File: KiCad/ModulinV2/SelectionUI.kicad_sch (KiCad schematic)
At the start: 43 parts, among them IC33 CD4028BM96, Q10 BC847B,215, Q11 BC847B,215, Q12 BC847B,215, Q13 BC847B,215, Q14 BC847B,215, Q15 BC847B,215, Q16 BC847B,215, Q17 BC847B,215, Q8 BC847B,215, Q9 BC847B,215

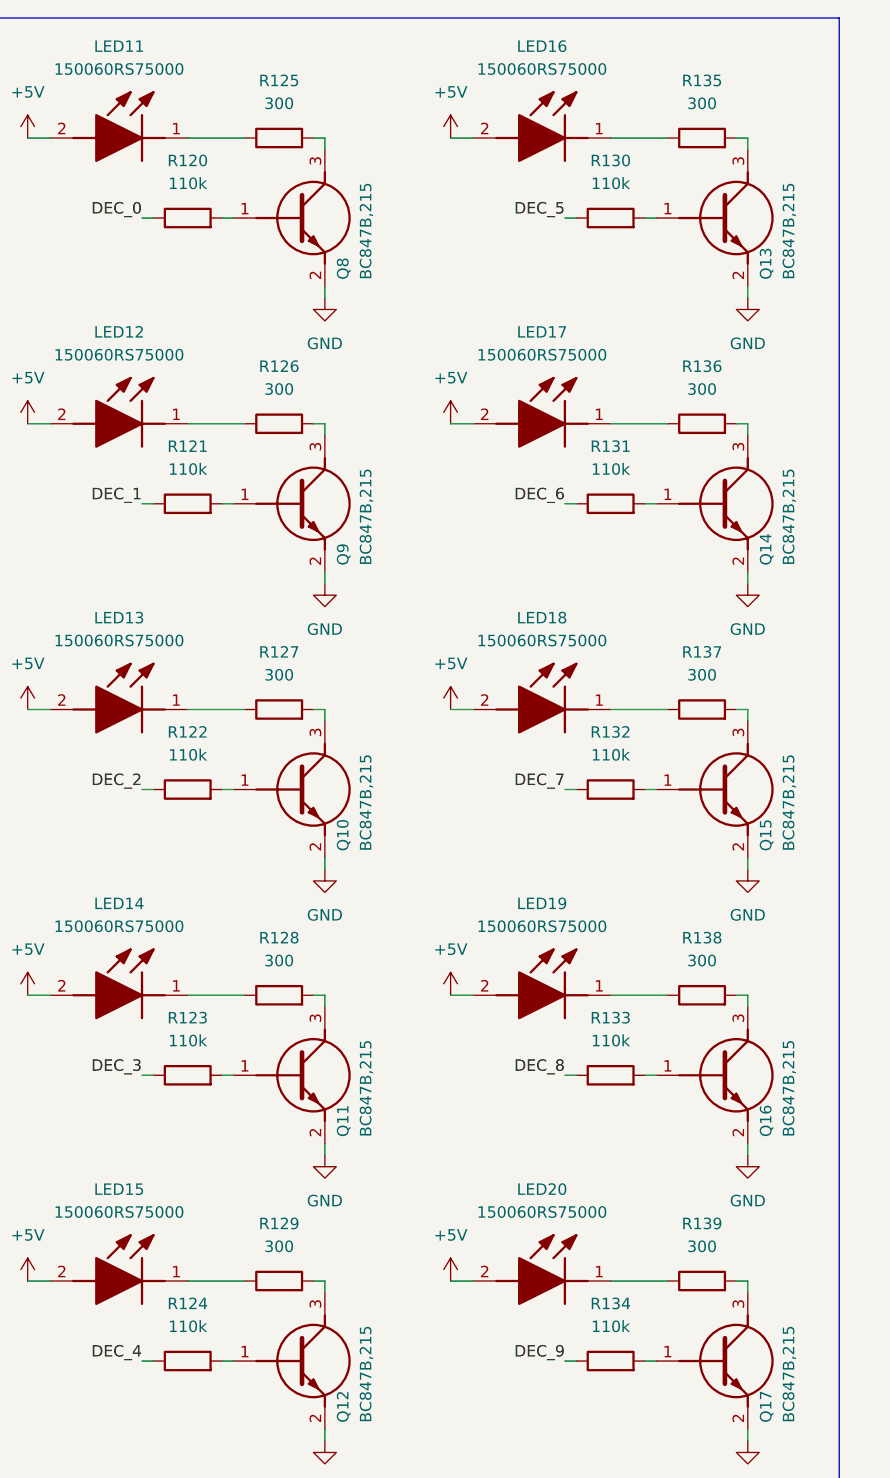
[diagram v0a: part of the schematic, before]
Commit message: Added 4k7 pullups to I2C lines
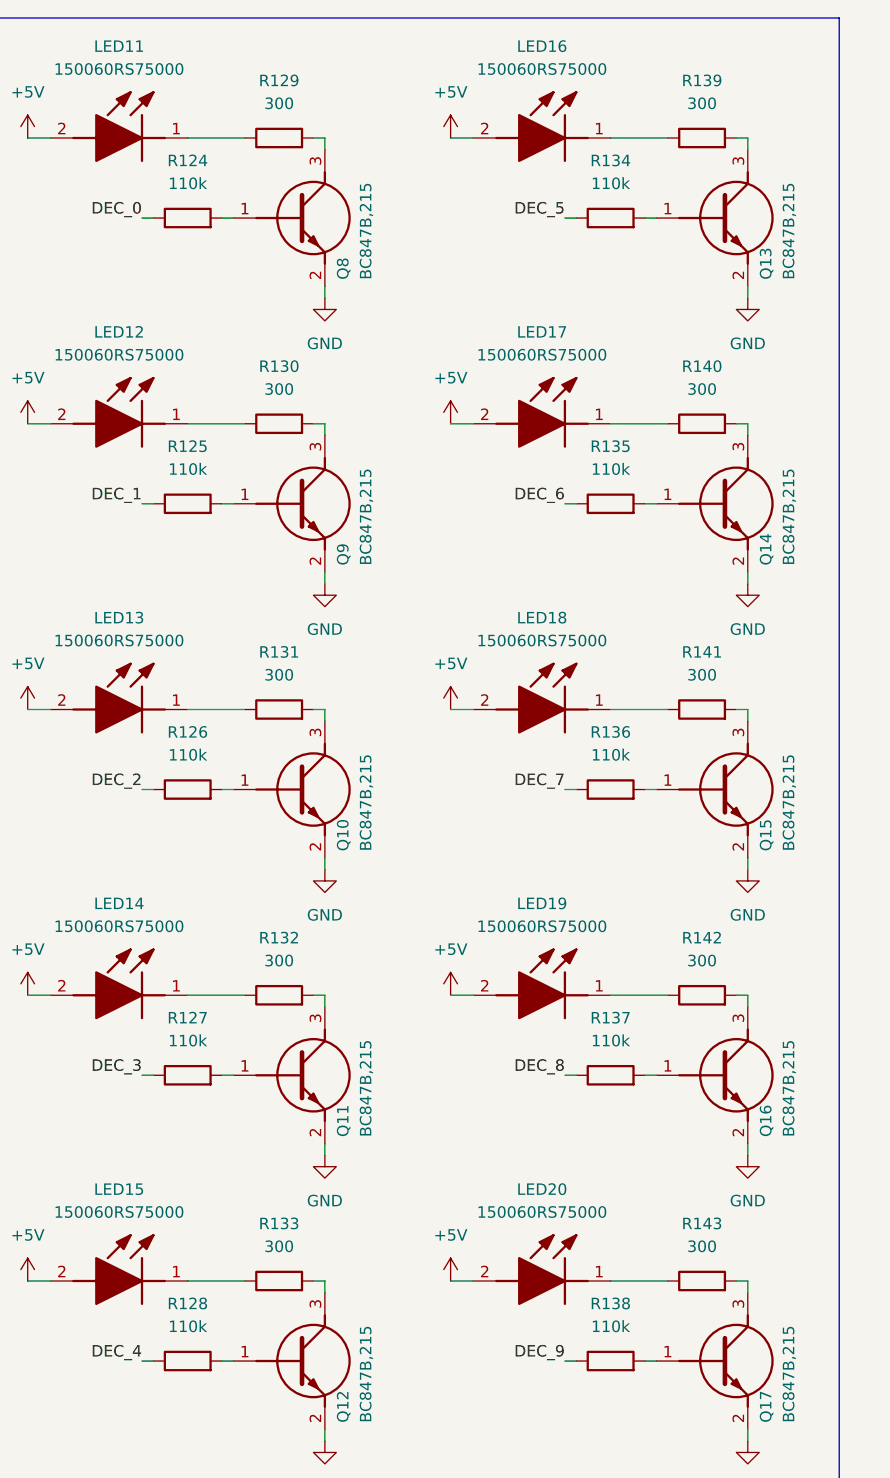
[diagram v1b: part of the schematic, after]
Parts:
- renumbered R120 to R124, R121 to R125, R122 to R126, R123 to R127, R124 to R128, R125 to R129, R126 to R130, R127 to R131, R128 to R132, R129 to R133, R130 to R134, R131 to R135, R132 to R136, R133 to R137, R134 to R138, R135 to R139, R136 to R140, R137 to R141, R138 to R142, R139 to R143

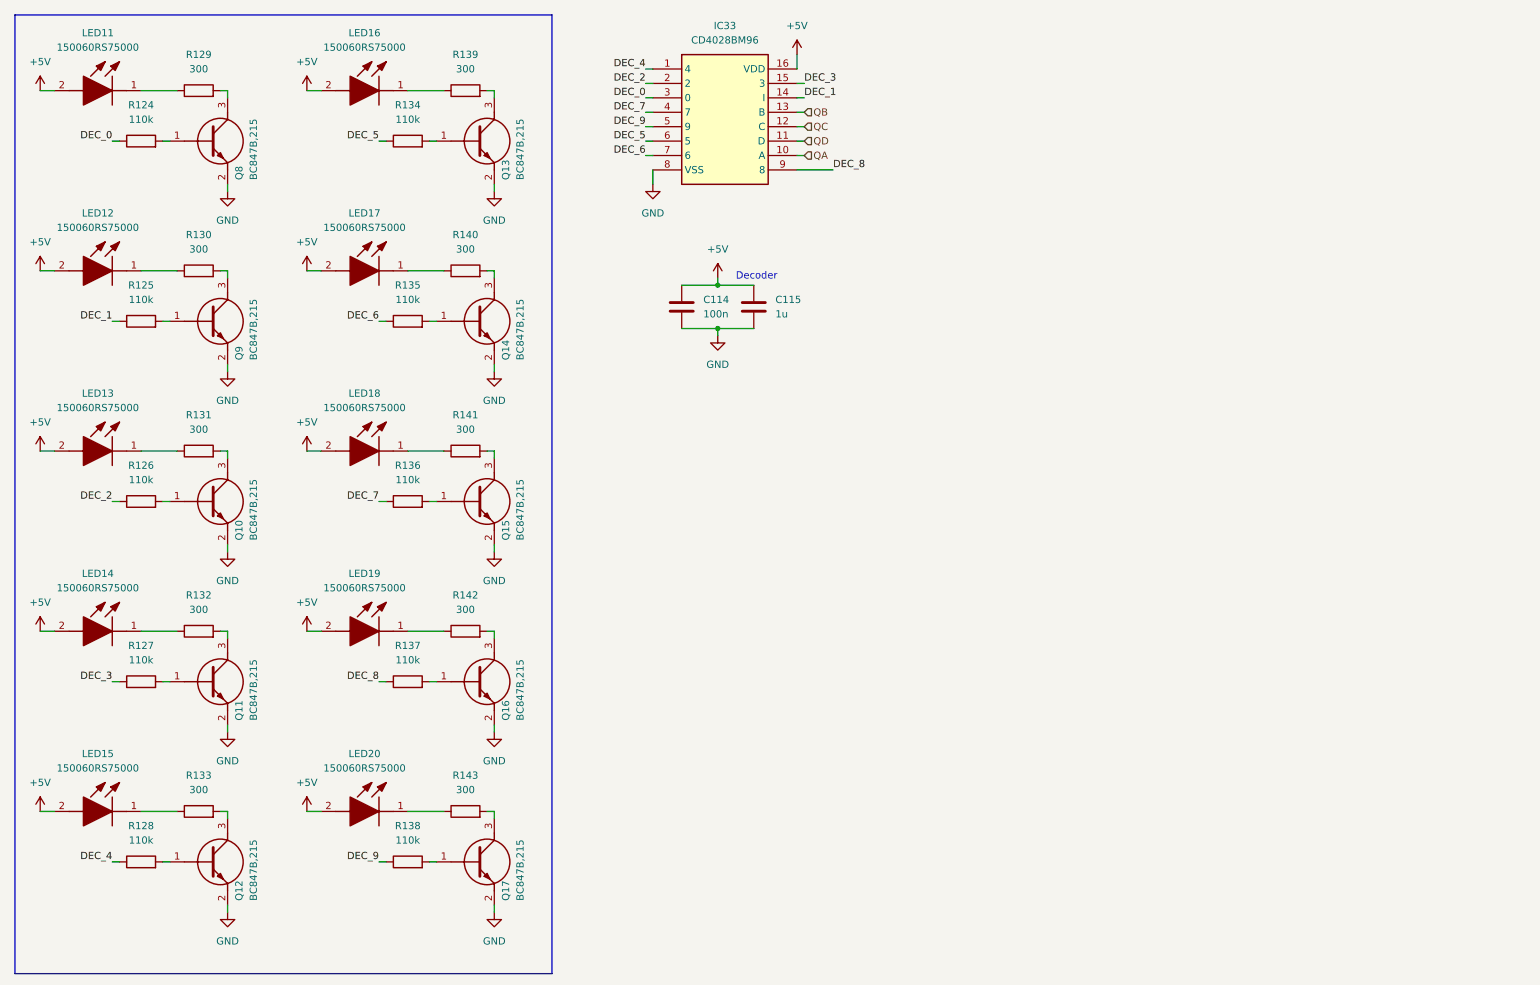
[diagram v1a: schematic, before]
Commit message: Added wave selection jumpers for testing
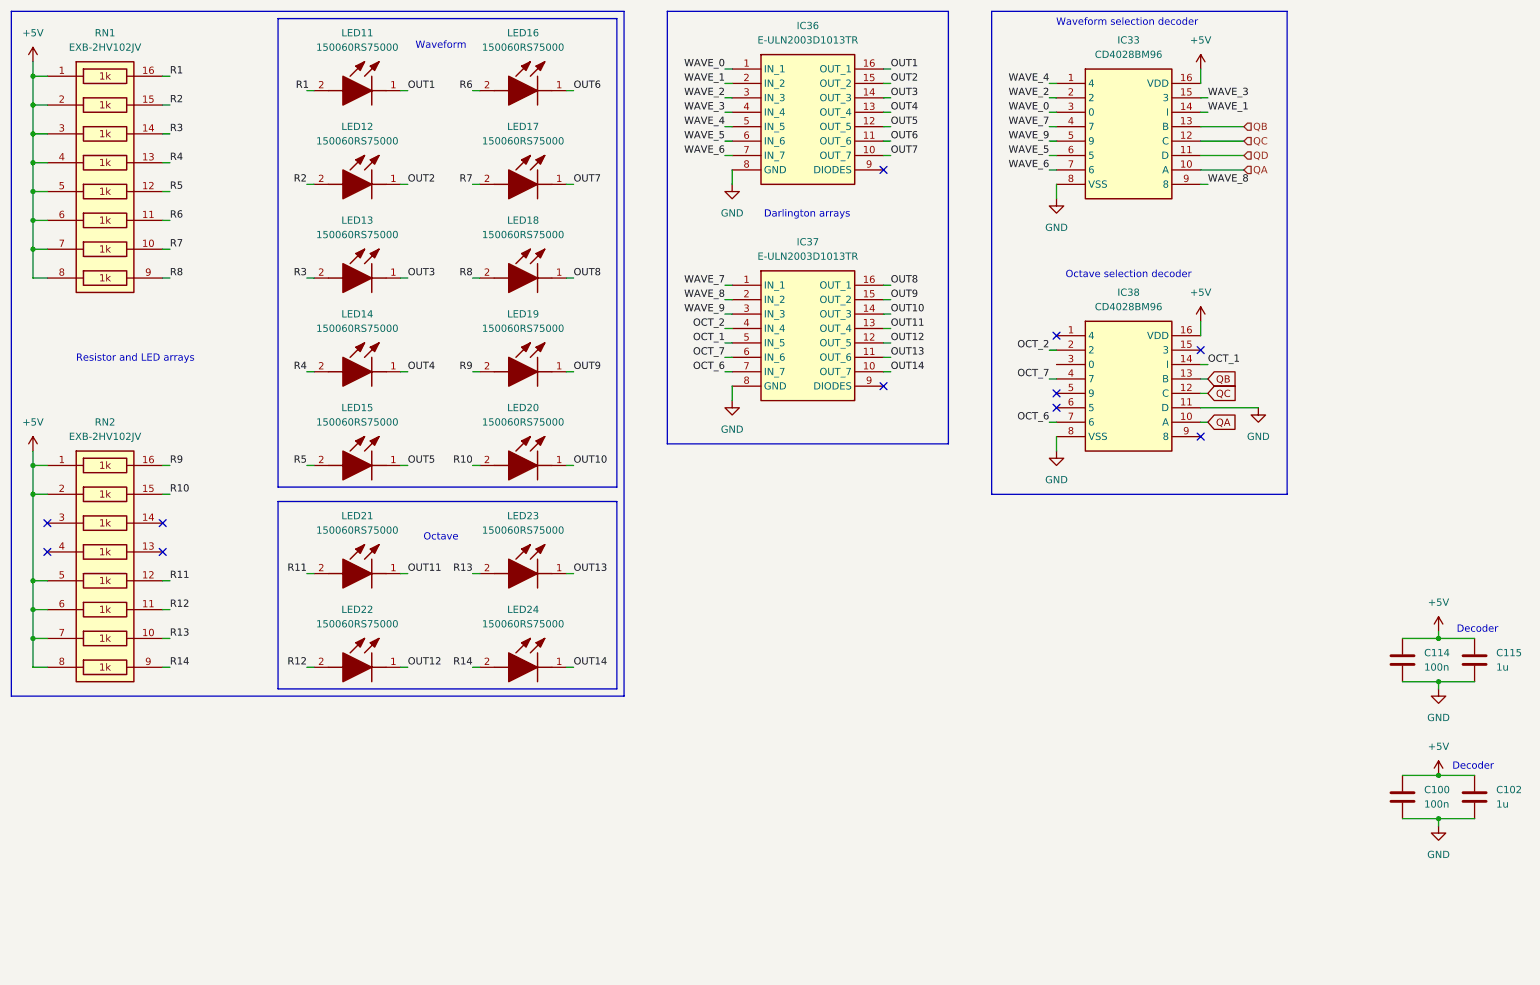
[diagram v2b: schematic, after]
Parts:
- removed Q10, Q11, Q12, Q13, Q14, Q15, Q16, Q17, Q8, Q9: BC847B,215, BC847B215, symbol BC847B_215:BC847B,215
- removed R124, R125, R126, R127, R128, R134, R135, R136, R137, R138: 110k, symbol Device:R
- removed R129, R130, R131, R132, R133, R139, R140, R141, R142, R143: 300, symbol Device:R
- added C100: 100n, symbol Device:C
- added C102: 1u, symbol Device:C
- added IC36, IC37: E-ULN2003D1013TR, SOIC127P600X175-16N, symbol E-ULN2003D1013TR:E-ULN2003D1013TR
- added IC38: CD4028BM96, SOIC127P600X175-16N, symbol CD4028BM96:CD4028BM96
- added LED21, LED22, LED23, LED24: 150060RS75000, LEDC1608X80N, symbol 150060RS75000:150060RS75000
- added RN1, RN2: EXB-2HV102JV, EXB2HV102JV, symbol EXB-2HV102JV:EXB-2HV102JV
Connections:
- net +5V: now also C100.2, C102.2, IC38.16 (VDD), RN1.1, RN1.2, RN1.3, RN1.4, RN1.5, RN1.6, RN1.7, RN1.8, RN2.1, RN2.2, RN2.5, RN2.6, RN2.7, RN2.8; no longer LED11.2 (A), LED12.2 (A), LED13.2 (A), LED14.2 (A), LED15.2 (A), LED16.2 (A), LED17.2 (A), LED18.2 (A), LED19.2 (A), LED20.2 (A)
- net GND: now also C100.1, C102.1, IC36.8 (GND), IC37.8 (GND), IC38.11 (D), IC38.8 (VSS)
- net QA: now also IC38.10 (A)
- net QB: now also IC38.13 (B)
- net QC: now also IC38.12 (C)
- net OUT2: now reaches LED12.1 (K)
- net OUT2: now also IC36.15 (OUT_2)
- net OUT9: now reaches LED19.1 (K)
- net OUT9: now also IC37.15 (OUT_2)
- net OUT4: now reaches LED14.1 (K)
- net OUT4: now also IC36.13 (OUT_4)
- net OUT1: now reaches LED11.1 (K)
- net OUT1: now also IC36.16 (OUT_1)
- net OUT7: now reaches LED17.1 (K)
- net OUT7: now also IC36.10 (OUT_7)
- net OUT8: now reaches LED18.1 (K)
- net OUT8: now also IC37.16 (OUT_1)
- net OUT5: now reaches LED15.1 (K)
- net OUT5: now also IC36.12 (OUT_5)
- net OUT3: now reaches LED13.1 (K)
- net OUT3: now also IC36.14 (OUT_3)
- net OUT6: now reaches LED16.1 (K)
- net OUT6: now also IC36.11 (OUT_6)
- net OUT10: now reaches LED20.1 (K)
- net OUT10: now also IC37.14 (OUT_3)
- net DEC_0 renamed WAVE_0
- net WAVE_0: now also IC36.1 (IN_1)
- net DEC_1 renamed WAVE_1
- net WAVE_1: now also IC36.2 (IN_2)
- net DEC_2 renamed WAVE_2
- net WAVE_2: now also IC36.3 (IN_3)
- net DEC_3 renamed WAVE_3
- net WAVE_3: now also IC36.4 (IN_4)
- net DEC_4 renamed WAVE_4
- net WAVE_4: now also IC36.5 (IN_5)
- net DEC_5 renamed WAVE_5
- net WAVE_5: now also IC36.6 (IN_6)
- net DEC_6 renamed WAVE_6
- net WAVE_6: now also IC36.7 (IN_7)
- net DEC_7 renamed WAVE_7
- net WAVE_7: now also IC37.1 (IN_1)
- net DEC_8 renamed WAVE_8
- net WAVE_8: now also IC37.2 (IN_2)
- net DEC_9 renamed WAVE_9
- net WAVE_9: now also IC37.3 (IN_3)
- new net OCT_1: IC37.5 (IN_5), IC38.14 (I)
- new net OCT_2: IC37.4 (IN_4), IC38.2
- new net OCT_6: IC37.7 (IN_7), IC38.7 (6)
- new net OCT_7: IC37.6 (IN_6), IC38.4 (7)
- new net OUT11: IC37.13 (OUT_4), LED21.1 (K)
- new net OUT12: IC37.12 (OUT_5), LED22.1 (K)
- new net OUT13: IC37.11 (OUT_6), LED23.1 (K)
- new net OUT14: IC37.10 (OUT_7), LED24.1 (K)
- new net R1: LED11.2 (A), RN1.16
- new net R10: LED20.2 (A), RN2.15
- new net R11: LED21.2 (A), RN2.12
- new net R12: LED22.2 (A), RN2.11
- new net R13: LED23.2 (A), RN2.10
- new net R14: LED24.2 (A), RN2.9
- new net R2: LED12.2 (A), RN1.15
- new net R3: LED13.2 (A), RN1.14
- new net R4: LED14.2 (A), RN1.13
- new net R5: LED15.2 (A), RN1.12
- new net R6: LED16.2 (A), RN1.11
- new net R7: LED17.2 (A), RN1.10
- new net R8: LED18.2 (A), RN1.9
- new net R9: LED19.2 (A), RN2.16
- no-connect marks 0 -> 11
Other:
- note added: "Darlington arrays"
- note added: "Octave"
- note added: "Octave selection decoder"
- note added: "Resistor and LED arrays"
- note added: "Waveform"
- note added: "Waveform selection decoder"
- moved on the sheet: C114, C115, IC33, LED11

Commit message: Revert "Modified selection LED schematic and supply caps"
This reverts commit f7ca9d31056dcb2cadf4048ae59e1f5625a2aefa.
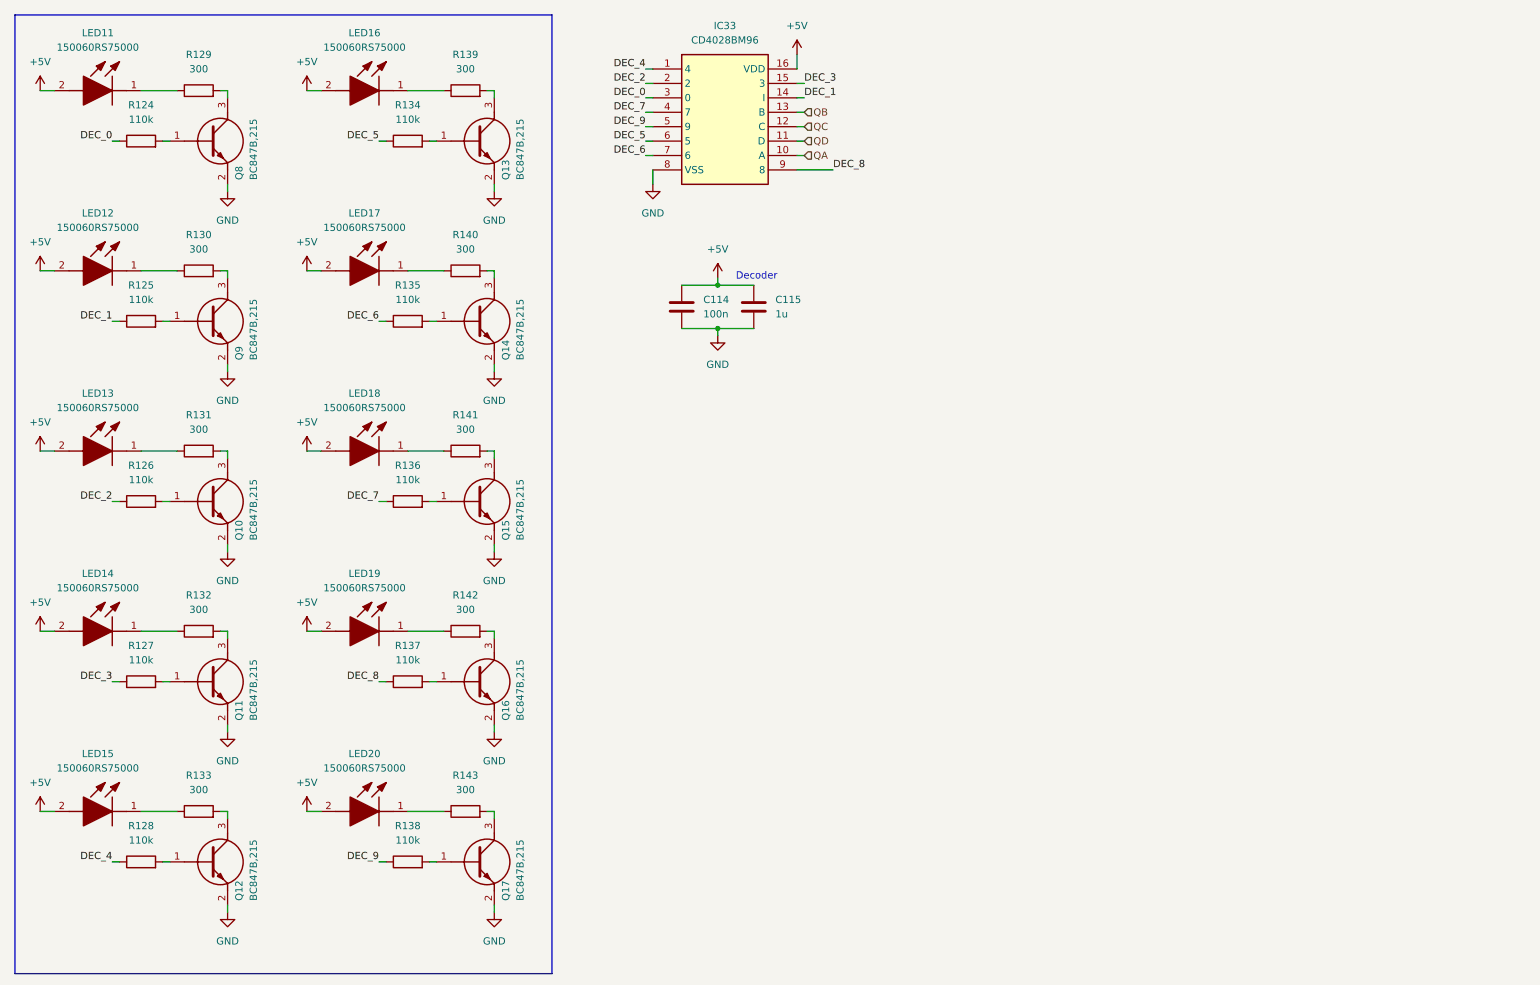
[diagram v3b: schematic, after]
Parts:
- removed C100: 100n, symbol Device:C
- removed C102: 1u, symbol Device:C
- removed IC36, IC37: E-ULN2003D1013TR, SOIC127P600X175-16N, symbol E-ULN2003D1013TR:E-ULN2003D1013TR
- removed IC38: CD4028BM96, SOIC127P600X175-16N, symbol CD4028BM96:CD4028BM96
- removed LED21, LED22, LED23, LED24: 150060RS75000, LEDC1608X80N, symbol 150060RS75000:150060RS75000
- removed RN1, RN2: EXB-2HV102JV, EXB2HV102JV, symbol EXB-2HV102JV:EXB-2HV102JV
- added Q10, Q11, Q12, Q13, Q14, Q15, Q16, Q17, Q8, Q9: BC847B,215, BC847B215, symbol BC847B_215:BC847B,215
- added R124, R125, R126, R127, R128, R134, R135, R136, R137, R138: 110k, symbol Device:R
- added R129, R130, R131, R132, R133, R139, R140, R141, R142, R143: 300, symbol Device:R
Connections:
- net R1 is gone; now on net +5V: LED11.2 (A)
- net R10 is gone; now on net +5V: LED20.2 (A)
- net R2 is gone; now on net +5V: LED12.2 (A)
- net R3 is gone; now on net +5V: LED13.2 (A)
- net R4 is gone; now on net +5V: LED14.2 (A)
- net R5 is gone; now on net +5V: LED15.2 (A)
- net R6 is gone; now on net +5V: LED16.2 (A)
- net R7 is gone; now on net +5V: LED17.2 (A)
- net R8 is gone; now on net +5V: LED18.2 (A)
- net R9 is gone; now on net +5V: LED19.2 (A)
- net GND: now also Q10.2 (E), Q11.2 (E), Q12.2 (E), Q13.2 (E), Q14.2 (E), Q15.2 (E), Q16.2 (E), Q17.2 (E), Q8.2 (E), Q9.2 (E)
- net OUT1: no longer names the net of LED11.1 (K)
- net OUT1: now also R129.1
- net OUT10: no longer names the net of LED20.1 (K)
- net OUT10: now also R143.1
- net OUT2: no longer names the net of LED12.1 (K)
- net OUT2: now also R130.1
- net OUT3: no longer names the net of LED13.1 (K)
- net OUT3: now also R131.1
- net OUT4: no longer names the net of LED14.1 (K)
- net OUT4: now also R132.1
- net OUT5: no longer names the net of LED15.1 (K)
- net OUT5: now also R133.1
- net OUT6: no longer names the net of LED16.1 (K)
- net OUT6: now also R139.1
- net OUT7: no longer names the net of LED17.1 (K)
- net OUT7: now also R140.1
- net OUT8: no longer names the net of LED18.1 (K)
- net OUT8: now also R141.1
- net OUT9: no longer names the net of LED19.1 (K)
- net OUT9: now also R142.1
- net WAVE_0 renamed DEC_0
- net DEC_0: now also R124.1
- net WAVE_1 renamed DEC_1
- net DEC_1: now also R125.1
- net WAVE_2 renamed DEC_2
- net DEC_2: now also R126.1
- net WAVE_3 renamed DEC_3
- net DEC_3: now also R127.1
- net WAVE_4 renamed DEC_4
- net DEC_4: now also R128.1
- net WAVE_5 renamed DEC_5
- net DEC_5: now also R134.1
- net WAVE_6 renamed DEC_6
- net DEC_6: now also R135.1
- net WAVE_7 renamed DEC_7
- net DEC_7: now also R136.1
- net WAVE_8 renamed DEC_8
- net DEC_8: now also R137.1
- net WAVE_9 renamed DEC_9
- net DEC_9: now also R138.1
- new net: Q10.1 (B), R126.2
- new net: Q9.1 (B), R125.2
- new net: Q9.3 (C), R130.2
- new net: Q16.3 (C), R142.2
- new net: Q8.1 (B), R124.2
- new net: Q8.3 (C), R129.2
- new net: Q13.1 (B), R134.2
- new net: Q12.1 (B), R128.2
- new net: Q11.3 (C), R132.2
- new net: Q12.3 (C), R133.2
- new net: Q10.3 (C), R131.2
- new net: Q17.1 (B), R138.2
- new net: Q17.3 (C), R143.2
- new net: Q14.3 (C), R140.2
- new net: Q14.1 (B), R135.2
- new net: Q13.3 (C), R139.2
- new net: Q16.1 (B), R137.2
- new net: Q11.1 (B), R127.2
- new net: Q15.3 (C), R141.2
- new net: Q15.1 (B), R136.2
- no-connect marks 11 -> 0
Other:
- note removed: "Darlington arrays"
- note removed: "Octave"
- note removed: "Octave selection decoder"
- note removed: "Resistor and LED arrays"
- note removed: "Waveform"
- note removed: "Waveform selection decoder"
- moved on the sheet: C114, C115, IC33, LED11
